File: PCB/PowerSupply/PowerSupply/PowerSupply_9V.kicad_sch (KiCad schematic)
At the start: 18 parts

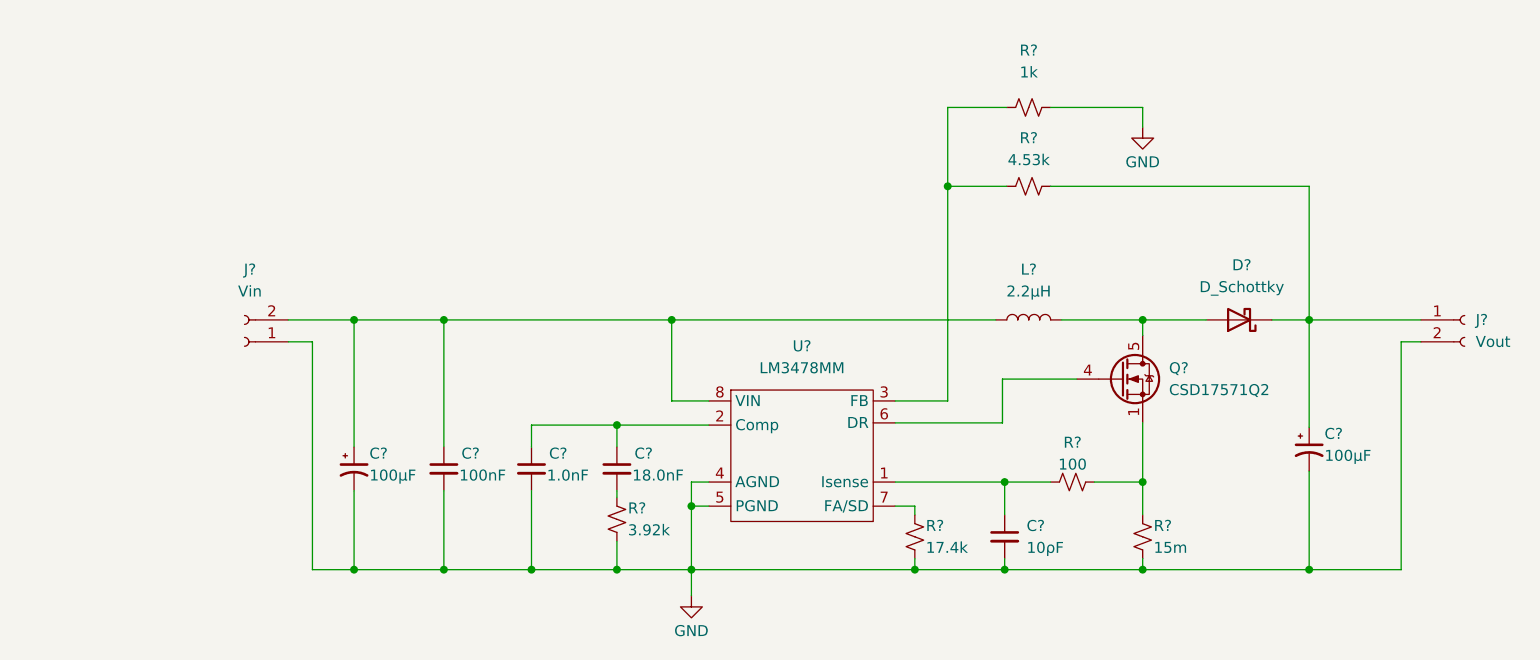
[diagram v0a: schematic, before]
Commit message: Finalized both power supply
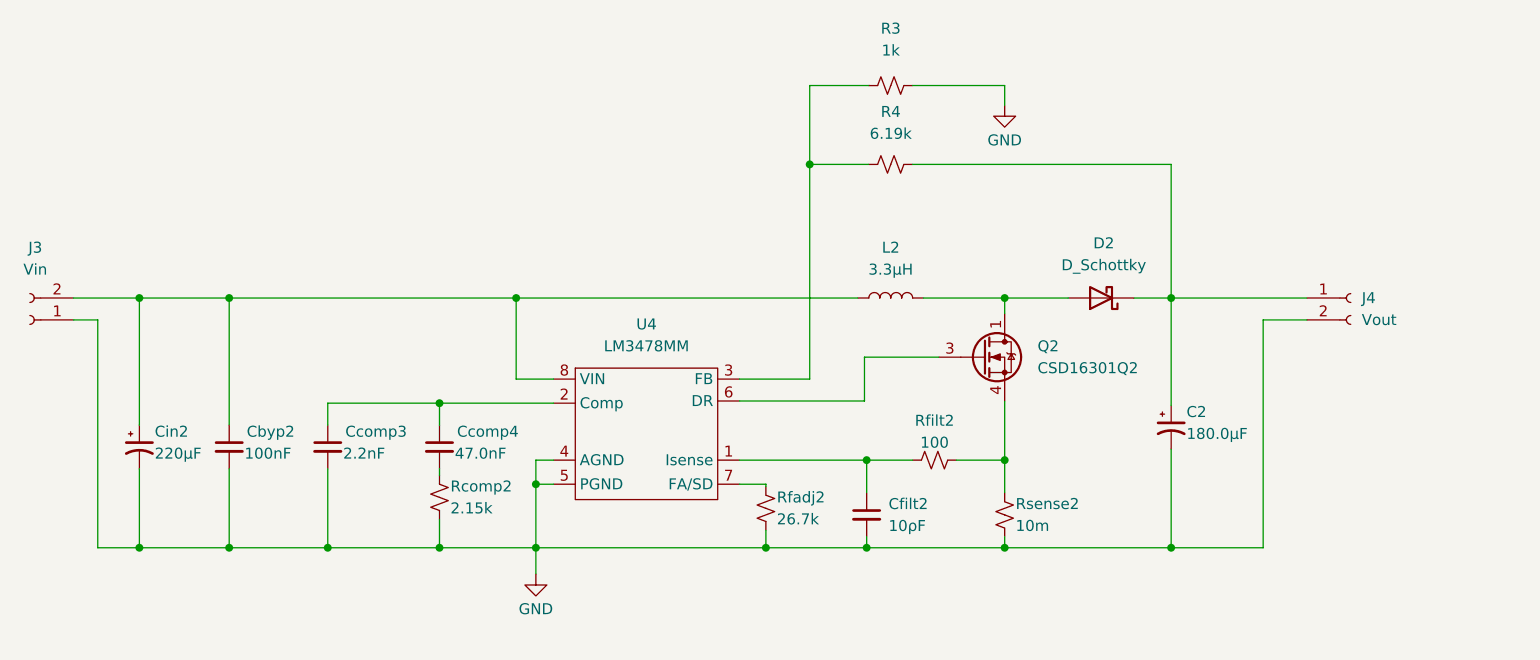
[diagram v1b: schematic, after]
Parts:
- removed C?: 18.0nF, Resistor_SMD:R_0402_1005Metric_Pad0.72x0.64mm_HandSolder, symbol Device:C_Small
- removed C?: 10ρF, Capacitor_SMD:C_0805_2012Metric_Pad1.18x1.45mm_HandSolder, symbol Device:C_Small
- removed C?: 100µF, Capacitor_SMD:CP_Elec_10x10, symbol Device:C_Polarized_Small_US
- removed C?: 100nF, Capacitor_SMD:C_0402_1005Metric_Pad0.74x0.62mm_HandSolder, symbol Device:C_Small
- removed C?: 100µF, Capacitor_SMD:C_0805_2012Metric_Pad1.18x1.45mm_HandSolder, symbol Device:C_Polarized_Small_US
- removed C?: 1.0nF, Capacitor_SMD:C_0805_2012Metric_Pad1.18x1.45mm_HandSolder, symbol Device:C_Small
- removed D?: D_Schottky, Diode_SMD:D_SMB-SMC_Universal_Handsoldering, symbol Device:D_Schottky
- removed J?: Vout, Connector_PinHeader_2.54mm:PinHeader_1x02_P2.54mm_Vertical, symbol Connector:Conn_01x02_Female
- removed J?: Vin, Connector_PinHeader_2.54mm:PinHeader_1x02_P2.54mm_Vertical, symbol Connector:Conn_01x02_Female
- removed L?: 2.2µH, Inductor_SMD:L_TDK_VLP8040, symbol Device:L
- removed Q?: CSD17571Q2, Package_SON:Texas_DQK, symbol Transistor_FET:CSD17579Q5A
- removed R?: 100, Resistor_SMD:R_0805_2012Metric_Pad1.20x1.40mm_HandSolder, symbol Device:R_Small_US
- removed R?: 15m, Resistor_SMD:R_1206_3216Metric_Pad1.30x1.75mm_HandSolder, symbol Device:R_Small_US
- removed R?: 4.53k, Resistor_SMD:R_0402_1005Metric_Pad0.72x0.64mm_HandSolder, symbol Device:R_Small_US
- removed R?: 1k, Resistor_SMD:R_0402_1005Metric_Pad0.72x0.64mm_HandSolder, symbol Device:R_Small_US
- removed R?: 3.92k, Resistor_SMD:R_0805_2012Metric_Pad1.20x1.40mm_HandSolder, symbol Device:R_Small_US
- removed R?: 17.4k, Resistor_SMD:R_0402_1005Metric_Pad0.72x0.64mm_HandSolder, symbol Device:R_Small_US
- removed U?: LM3478MM, Package_SO:SOIC-8-1EP_3.9x4.9mm_P1.27mm_EP2.29x3mm, symbol CustomPower:LM3478MM
- added C2: 180.0μF, Capacitor_SMD:CP_Elec_10x10, symbol Device:C_Polarized_Small_US
- added Cbyp2: 100nF, Capacitor_SMD:C_0402_1005Metric_Pad0.74x0.62mm_HandSolder, symbol Device:C_Small
- added Ccomp3: 2.2nF, Capacitor_SMD:C_0805_2012Metric_Pad1.18x1.45mm_HandSolder, symbol Device:C_Small
- added Ccomp4: 47.0nF, Resistor_SMD:R_0402_1005Metric_Pad0.72x0.64mm_HandSolder, symbol Device:C_Small
- added Cfilt2: 10ρF, Capacitor_SMD:C_0805_2012Metric_Pad1.18x1.45mm_HandSolder, symbol Device:C_Small
- added Cin2: 220µF, Capacitor_SMD:C_0805_2012Metric_Pad1.18x1.45mm_HandSolder, symbol Device:C_Polarized_Small_US
- added D2: D_Schottky, Diode_SMD:D_SMB-SMC_Universal_Handsoldering, symbol Device:D_Schottky
- added J3: Vin, Connector_PinHeader_2.54mm:PinHeader_1x02_P2.54mm_Vertical, symbol Connector:Conn_01x02_Female
- added J4: Vout, Connector_PinHeader_2.54mm:PinHeader_1x02_P2.54mm_Vertical, symbol Connector:Conn_01x02_Female
- added L2: 3.3µH, Inductor_SMD:L_TDK_VLP8040, symbol Device:L
- added Q2: CSD16301Q2, Package_SON:Texas_DQK, symbol Transistor_FET:CSD16301Q2
- added R3: 1k, Resistor_SMD:R_0402_1005Metric_Pad0.72x0.64mm_HandSolder, symbol Device:R_Small_US
- added R4: 6.19k, Resistor_SMD:R_0402_1005Metric_Pad0.72x0.64mm_HandSolder, symbol Device:R_Small_US
- added Rcomp2: 2.15k, Resistor_SMD:R_0805_2012Metric_Pad1.20x1.40mm_HandSolder, symbol Device:R_Small_US
- added Rfadj2: 26.7k, Resistor_SMD:R_0402_1005Metric_Pad0.72x0.64mm_HandSolder, symbol Device:R_Small_US
- added Rfilt2: 100, Resistor_SMD:R_0805_2012Metric_Pad1.20x1.40mm_HandSolder, symbol Device:R_Small_US
- added Rsense2: 10m, Resistor_SMD:R_1206_3216Metric_Pad1.30x1.75mm_HandSolder, symbol Device:R_Small_US
- added U4: LM3478MM, Package_SO:SOIC-8-1EP_3.9x4.9mm_P1.27mm_EP2.29x3mm, symbol CustomPower:LM3478MM
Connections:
- net GND: now also C2.2, Cbyp2.2, Ccomp3.2, Cfilt2.2, Cin2.2, J3.1 (Pin_1), J4.2 (Pin_2), R3.2, Rcomp2.2, Rfadj2.2, Rsense2.2, U4.4 (AGND), U4.5 (PGND)
- new net: Cfilt2.1, Rfilt2.1, U4.1 (Isense)
- new net: Ccomp3.1, Ccomp4.1, U4.2 (Comp)
- new net: R3.1, R4.1, U4.3 (FB)
- new net: Q2.3 (G), U4.6 (DR)
- new net: Rfadj2.1, U4.7 (FA/SD)
- new net: Cbyp2.1, Cin2.1, J3.2 (Pin_2), L2.1, U4.8 (VIN)
- new net: Ccomp4.2, Rcomp2.1
- new net: Q2.4 (S), Q2.7 (S), Rfilt2.2, Rsense2.1
- new net: C2.1, D2.1 (K), J4.1 (Pin_1), R4.2
- new net: D2.2 (A), L2.2, Q2.1 (D), Q2.2 (D), Q2.5 (D), Q2.6 (D), Q2.8 (D)

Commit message: Fixed Zach's Stuff
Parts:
- R4: value 6.19k -> 3.74k
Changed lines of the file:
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@@
     (in_bom yes) (on_board yes) (fields_autoplaced)
     (property "Reference" "R4" (id 0) (at 152.4 71.12 90))
-    (property "Value" "6.19k" (id 1) (at 152.4 73.66 90))
+    (property "Value" "3.74k" (id 1) (at 152.4 73.66 90))
     (property "Footprint" "Resistor_SMD:R_0402_1005Metric_Pad0.72x0.64mm_HandSolder" (id 2) (at 152.4 77.216 0)
       (effects (font (size 1.27 1.27)) hide)

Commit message: Fixed Zach's errors :/ smh
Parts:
- added J5: Vout, Connector_PinHeader_2.54mm:PinHeader_1x02_P2.54mm_Vertical, symbol Connector:Conn_01x02_Female
- Cbyp2: footprint Capacitor_SMD:C_0402_1005Metric_Pad0.74x0.62mm_HandSolder -> Capacitor_SMD:C_0805_2012Metric_Pad1.18x1.45mm_HandSolder
- Ccomp4, R3, R4, Rfadj2: footprint Resistor_SMD:R_0402_1005Metric_Pad0.72x0.64mm_HandSolder -> Resistor_SMD:R_0805_2012Metric_Pad1.20x1.40mm_HandSolder
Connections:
- net GND: now also J5.2 (Pin_2)
- net at C2.1, D2.1 (K), J4.1 (Pin_1)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: now also J5.1 (Pin_1)
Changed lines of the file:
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@@
   (junction (at 100.076 104.902) (diameter 0) (color 0 0 0 0)
   )
+  (junction (at 195.58 100.584) (diameter 0) (color 0 0 0 0)
+  )
   (junction (at 165.608 121.666) (diameter 0) (color 0 0 0 0)
   )
@@
   (junction (at 87.122 121.666) (diameter 0) (color 0 0 0 0)
   )
+  (junction (at 184.912 98.044) (diameter 0) (color 0 0 0 0)
+  )
   (junction (at 75.692 121.666) (diameter 0) (color 0 0 0 0)
   )
@@
     (stroke (width 0) (type default) (color 0 0 0 0))
   )
-  (wire (pts (xy 184.912 92.71) (xy 184.912 105.156))
+  (wire (pts (xy 184.912 92.71) (xy 184.912 98.044))
     (stroke (width 0) (type default) (color 0 0 0 0))
   )
@@
     (stroke (width 0) (type default) (color 0 0 0 0))
   )
+  (wire (pts (xy 195.58 100.584) (xy 195.58 121.666))
+    (stroke (width 0) (type default) (color 0 0 0 0))
+  )
   (wire (pts (xy 180.594 92.71) (xy 184.912 92.71))
     (stroke (width 0) (type default) (color 0 0 0 0))
@@
     (stroke (width 0) (type default) (color 0 0 0 0))
   )
+  (wire (pts (xy 184.912 98.044) (xy 184.912 105.156))
+    (stroke (width 0) (type default) (color 0 0 0 0))
+  )
   (wire (pts (xy 60.452 121.666) (xy 65.278 121.666))
     (stroke (width 0) (type default) (color 0 0 0 0))
@@
     (stroke (width 0) (type default) (color 0 0 0 0))
   )
-  (wire (pts (xy 195.58 95.25) (xy 195.58 121.666))
+  (wire (pts (xy 195.58 95.25) (xy 195.58 100.584))
     (stroke (width 0) (type default) (color 0 0 0 0))
   )
@@
     (stroke (width 0) (type default) (color 0 0 0 0))
   )
+  (wire (pts (xy 184.912 98.044) (xy 200.66 98.044))
+    (stroke (width 0) (type default) (color 0 0 0 0))
+  )
   (wire (pts (xy 149.86 68.072) (xy 143.002 68.072))
     (stroke (width 0) (type default) (color 0 0 0 0))
@@
     (stroke (width 0) (type default) (color 0 0 0 0))
   )
+  (wire (pts (xy 195.58 100.584) (xy 200.66 100.584))
+    (stroke (width 0) (type default) (color 0 0 0 0))
+  )
   (wire (pts (xy 134.874 114.3) (xy 137.922 114.3))
     (stroke (width 0) (type default) (color 0 0 0 0))
@@
   (wire (pts (xy 108.966 92.71) (xy 108.966 102.108))
     (stroke (width 0) (type default) (color 0 0 0 0))
+  )
+  (symbol (lib_id "Connector:Conn_01x02_Female") (at 205.74 98.044 0) (unit 1)
+    (in_bom yes) (on_board yes) (fields_autoplaced)
+    (property "Reference" "J5" (id 0) (at 207.01 98.0439 0)
+      (effects (font (size 1.27 1.27)) (justify left))
+    )
+    (property "Value" "Vout" (id 1) (at 207.01 100.5839 0)
+      (effects (font (size 1.27 1.27)) (justify left))
+    )
+    (property "Footprint" "Connector_PinHeader_2.54mm:PinHeader_1x02_P2.54mm_Vertical" (id 2) (at 205.74 98.044 0)
+      (effects (font (size 1.27 1.27)) hide)
+    )
+    (property "Datasheet" "~" (id 3) (at 205.74 98.044 0)
+      (effects (font (size 1.27 1.27)) hide)
+    )
+    (pin "1")
+    (pin "2")
   )
   (symbol (lib_id "CustomPower:LM3478MM") (at 123.444 95.758 0) (unit 1)
@@
     (property "Reference" "R4" (id 0) (at 152.4 71.12 90))
     (property "Value" "3.74k" (id 1) (at 152.4 73.66 90))
-    (property "Footprint" "Resistor_SMD:R_0402_1005Metric_Pad0.72x0.64mm_HandSolder" (id 2) (at 152.4 77.216 0)
+    (property "Footprint" "Resistor_SMD:R_0805_2012Metric_Pad1.20x1.40mm_HandSolder" (id 2) (at 152.4 77.216 0)
       (effects (font (size 1.27 1.27)) hide)
     )
@@
     (property "Reference" "R3" (id 0) (at 152.4 61.468 90))
     (property "Value" "1k" (id 1) (at 152.4 64.008 90))
-    (property "Footprint" "Resistor_SMD:R_0402_1005Metric_Pad0.72x0.64mm_HandSolder" (id 2) (at 152.4 68.072 0)
+    (property "Footprint" "Resistor_SMD:R_0805_2012Metric_Pad1.20x1.40mm_HandSolder" (id 2) (at 152.4 68.072 0)
       (effects (font (size 1.27 1.27)) hide)
     )
@@
       (effects (font (size 1.27 1.27)) (justify left))
     )
-    (property "Footprint" "Resistor_SMD:R_0402_1005Metric_Pad0.72x0.64mm_HandSolder" (id 2) (at 137.922 117.094 0)
+    (property "Footprint" "Resistor_SMD:R_0805_2012Metric_Pad1.20x1.40mm_HandSolder" (id 2) (at 137.922 117.094 0)
       (effects (font (size 1.27 1.27)) hide)
     )
@@
       (effects (font (size 1.27 1.27)) (justify left))
     )
-    (property "Footprint" "Capacitor_SMD:C_0402_1005Metric_Pad0.74x0.62mm_HandSolder" (id 2) (at 75.692 109.982 0)
+    (property "Footprint" "Capacitor_SMD:C_0805_2012Metric_Pad1.18x1.45mm_HandSolder" (id 2) (at 75.692 109.982 0)
       (effects (font (size 1.27 1.27)) hide)
     )
@@
       (effects (font (size 1.27 1.27)) (justify left))
     )
-    (property "Footprint" "Resistor_SMD:R_0402_1005Metric_Pad0.72x0.64mm_HandSolder" (id 2) (at 100.076 109.982 0)
-      (effects (font (size 1.27 1.27)) hide)
-    )
+    (property "Footprint" "Resistor_SMD:R_0805_2012Metric_Pad1.20x1.40mm_HandSolder" (id 2) (at 100.076 109.982 0)
+      (effects (font (size 1.27 1.27)) hide)
+    )
